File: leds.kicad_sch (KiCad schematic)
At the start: 67 parts, among them U4 TXB0101DRL

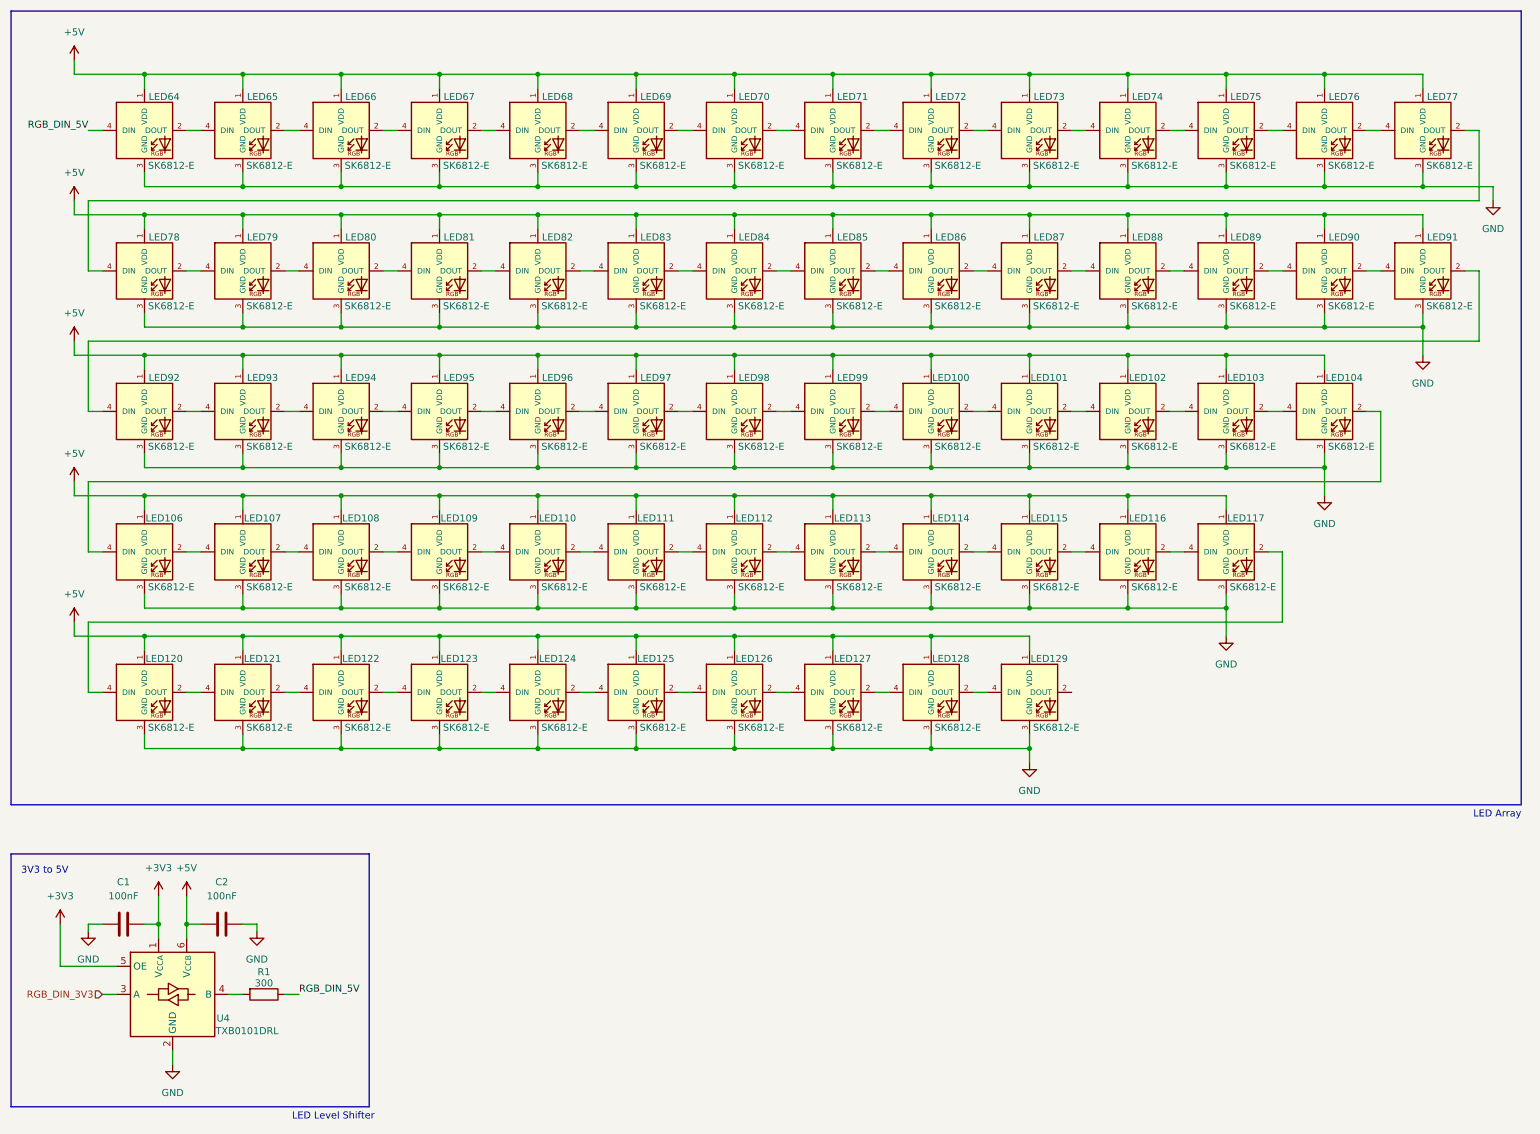
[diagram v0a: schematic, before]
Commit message: created v0.2 pcb
Started work on v0.2 pcb. Placed switches, LEDS, and Diodes. Working on MCU routing
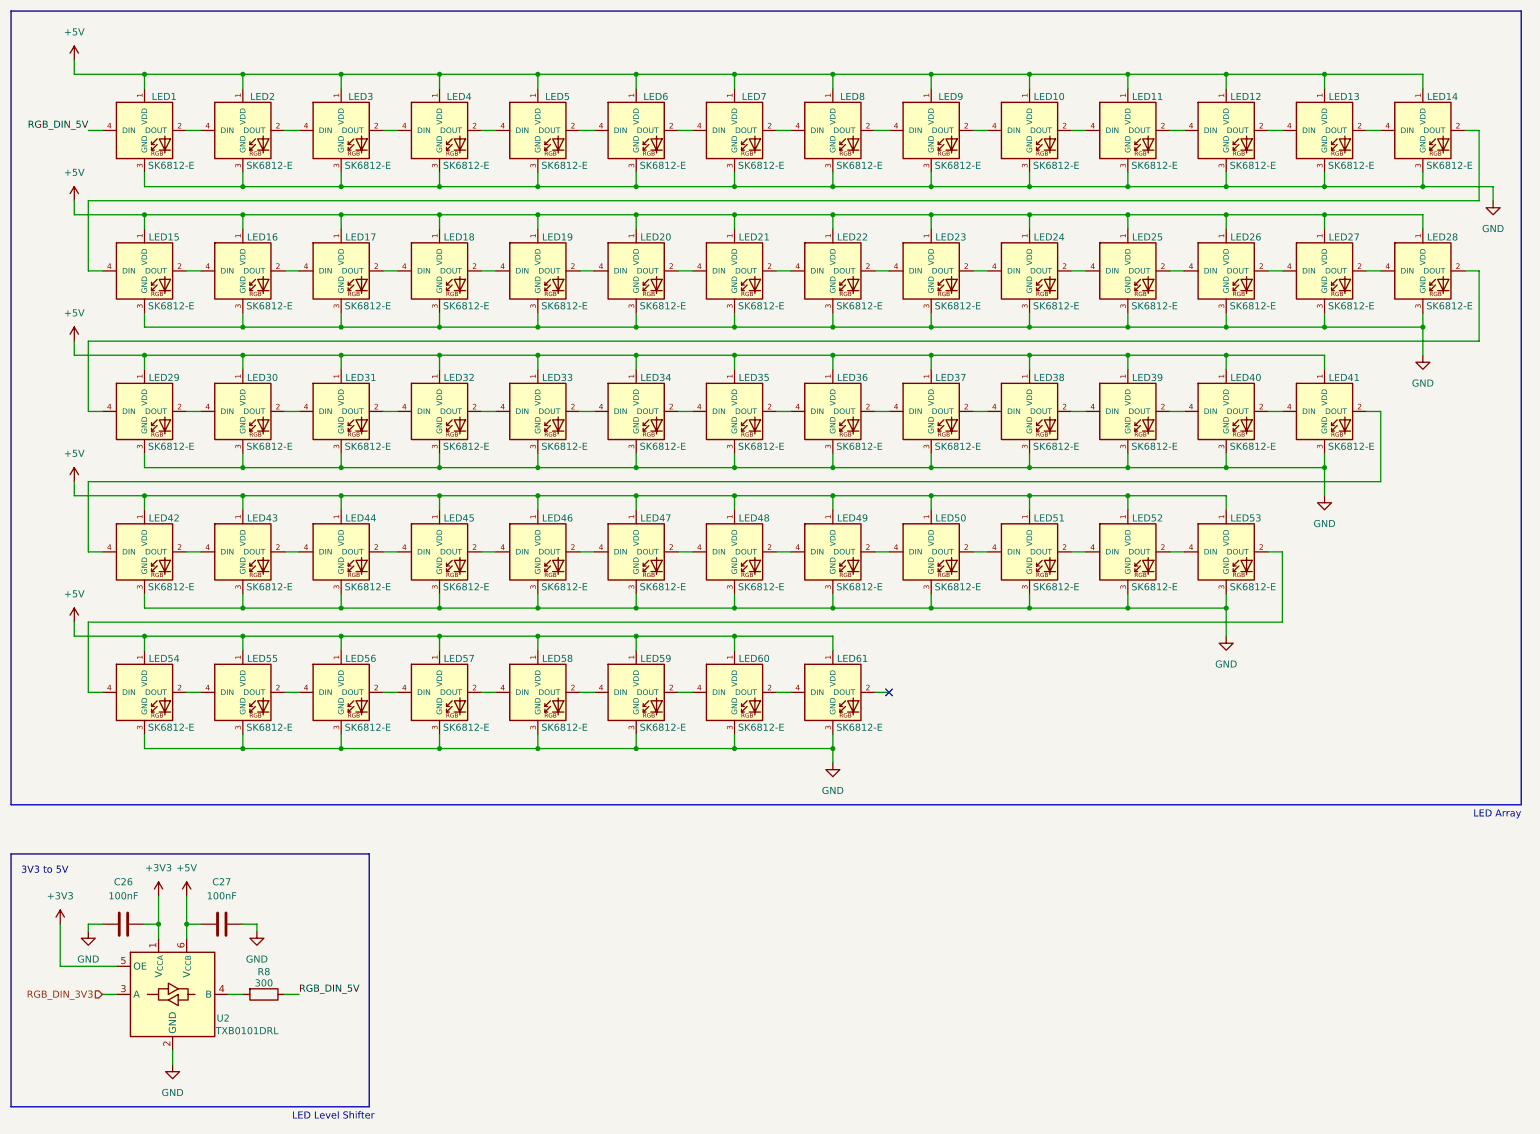
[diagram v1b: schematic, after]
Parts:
- removed LED128, LED129: SK6812-E, SK6812-E:LED_SK6812-E, symbol SK6812-E:SK6812-E
- C26: renamed from C1; footprint (none) -> Capacitor_SMD:C_0402_1005Metric
- C27: renamed from C2; footprint (none) -> Capacitor_SMD:C_0402_1005Metric
- LED1: renamed from LED64; footprint SK6812-E:LED_SK6812-E -> SamacSys_Parts:LED_SK6812-E
- LED10: renamed from LED73; footprint SK6812-E:LED_SK6812-E -> SamacSys_Parts:LED_SK6812-E
- LED11: renamed from LED74; footprint SK6812-E:LED_SK6812-E -> SamacSys_Parts:LED_SK6812-E
- LED12: renamed from LED75; footprint SK6812-E:LED_SK6812-E -> SamacSys_Parts:LED_SK6812-E
- LED13: renamed from LED76; footprint SK6812-E:LED_SK6812-E -> SamacSys_Parts:LED_SK6812-E
- LED14: renamed from LED77; footprint SK6812-E:LED_SK6812-E -> SamacSys_Parts:LED_SK6812-E
- LED15: renamed from LED78; footprint SK6812-E:LED_SK6812-E -> SamacSys_Parts:LED_SK6812-E
- LED16: renamed from LED79; footprint SK6812-E:LED_SK6812-E -> SamacSys_Parts:LED_SK6812-E
- LED17: renamed from LED80; footprint SK6812-E:LED_SK6812-E -> SamacSys_Parts:LED_SK6812-E
- LED18: renamed from LED81; footprint SK6812-E:LED_SK6812-E -> SamacSys_Parts:LED_SK6812-E
- LED19: renamed from LED82; footprint SK6812-E:LED_SK6812-E -> SamacSys_Parts:LED_SK6812-E
- LED2: renamed from LED65; footprint SK6812-E:LED_SK6812-E -> SamacSys_Parts:LED_SK6812-E
- LED20: renamed from LED83; footprint SK6812-E:LED_SK6812-E -> SamacSys_Parts:LED_SK6812-E
- LED21: renamed from LED84; footprint SK6812-E:LED_SK6812-E -> SamacSys_Parts:LED_SK6812-E
- LED22: renamed from LED85; footprint SK6812-E:LED_SK6812-E -> SamacSys_Parts:LED_SK6812-E
- LED23: renamed from LED86; footprint SK6812-E:LED_SK6812-E -> SamacSys_Parts:LED_SK6812-E
- LED24: renamed from LED87; footprint SK6812-E:LED_SK6812-E -> SamacSys_Parts:LED_SK6812-E
- LED25: renamed from LED88; footprint SK6812-E:LED_SK6812-E -> SamacSys_Parts:LED_SK6812-E
- LED26: renamed from LED89; footprint SK6812-E:LED_SK6812-E -> SamacSys_Parts:LED_SK6812-E
- LED27: renamed from LED90; footprint SK6812-E:LED_SK6812-E -> SamacSys_Parts:LED_SK6812-E
- LED28: renamed from LED91; footprint SK6812-E:LED_SK6812-E -> SamacSys_Parts:LED_SK6812-E
- LED29: renamed from LED92; footprint SK6812-E:LED_SK6812-E -> SamacSys_Parts:LED_SK6812-E
- LED3: renamed from LED66; footprint SK6812-E:LED_SK6812-E -> SamacSys_Parts:LED_SK6812-E
- LED30: renamed from LED93; footprint SK6812-E:LED_SK6812-E -> SamacSys_Parts:LED_SK6812-E
- LED31: renamed from LED94; footprint SK6812-E:LED_SK6812-E -> SamacSys_Parts:LED_SK6812-E
- LED32: renamed from LED95; footprint SK6812-E:LED_SK6812-E -> SamacSys_Parts:LED_SK6812-E
- LED33: renamed from LED96; footprint SK6812-E:LED_SK6812-E -> SamacSys_Parts:LED_SK6812-E
- LED34: renamed from LED97; footprint SK6812-E:LED_SK6812-E -> SamacSys_Parts:LED_SK6812-E
- LED35: renamed from LED98; footprint SK6812-E:LED_SK6812-E -> SamacSys_Parts:LED_SK6812-E
- LED36: renamed from LED99; footprint SK6812-E:LED_SK6812-E -> SamacSys_Parts:LED_SK6812-E
- LED37: renamed from LED100; footprint SK6812-E:LED_SK6812-E -> SamacSys_Parts:LED_SK6812-E
- LED38: renamed from LED101; footprint SK6812-E:LED_SK6812-E -> SamacSys_Parts:LED_SK6812-E
- LED39: renamed from LED102; footprint SK6812-E:LED_SK6812-E -> SamacSys_Parts:LED_SK6812-E
- LED4: renamed from LED67; footprint SK6812-E:LED_SK6812-E -> SamacSys_Parts:LED_SK6812-E
- LED40: renamed from LED103; footprint SK6812-E:LED_SK6812-E -> SamacSys_Parts:LED_SK6812-E
- LED41: renamed from LED104; footprint SK6812-E:LED_SK6812-E -> SamacSys_Parts:LED_SK6812-E
- LED42: renamed from LED106; footprint SK6812-E:LED_SK6812-E -> SamacSys_Parts:LED_SK6812-E
- LED43: renamed from LED107; footprint SK6812-E:LED_SK6812-E -> SamacSys_Parts:LED_SK6812-E
- LED44: renamed from LED108; footprint SK6812-E:LED_SK6812-E -> SamacSys_Parts:LED_SK6812-E
- LED45: renamed from LED109; footprint SK6812-E:LED_SK6812-E -> SamacSys_Parts:LED_SK6812-E
- LED46: renamed from LED110; footprint SK6812-E:LED_SK6812-E -> SamacSys_Parts:LED_SK6812-E
- LED47: renamed from LED111; footprint SK6812-E:LED_SK6812-E -> SamacSys_Parts:LED_SK6812-E
- LED48: renamed from LED112; footprint SK6812-E:LED_SK6812-E -> SamacSys_Parts:LED_SK6812-E
- LED49: renamed from LED113; footprint SK6812-E:LED_SK6812-E -> SamacSys_Parts:LED_SK6812-E
- LED5: renamed from LED68; footprint SK6812-E:LED_SK6812-E -> SamacSys_Parts:LED_SK6812-E
- LED50: renamed from LED114; footprint SK6812-E:LED_SK6812-E -> SamacSys_Parts:LED_SK6812-E
- LED51: renamed from LED115; footprint SK6812-E:LED_SK6812-E -> SamacSys_Parts:LED_SK6812-E
- LED52: renamed from LED116; footprint SK6812-E:LED_SK6812-E -> SamacSys_Parts:LED_SK6812-E
- LED53: renamed from LED117; footprint SK6812-E:LED_SK6812-E -> SamacSys_Parts:LED_SK6812-E
- LED54: renamed from LED120; footprint SK6812-E:LED_SK6812-E -> SamacSys_Parts:LED_SK6812-E
- LED55: renamed from LED121; footprint SK6812-E:LED_SK6812-E -> SamacSys_Parts:LED_SK6812-E
- LED56: renamed from LED122; footprint SK6812-E:LED_SK6812-E -> SamacSys_Parts:LED_SK6812-E
- LED57: renamed from LED123; footprint SK6812-E:LED_SK6812-E -> SamacSys_Parts:LED_SK6812-E
- LED58: renamed from LED124; footprint SK6812-E:LED_SK6812-E -> SamacSys_Parts:LED_SK6812-E
- LED59: renamed from LED125; footprint SK6812-E:LED_SK6812-E -> SamacSys_Parts:LED_SK6812-E
- LED6: renamed from LED69; footprint SK6812-E:LED_SK6812-E -> SamacSys_Parts:LED_SK6812-E
- LED60: renamed from LED126; footprint SK6812-E:LED_SK6812-E -> SamacSys_Parts:LED_SK6812-E
- LED61: renamed from LED127; footprint SK6812-E:LED_SK6812-E -> SamacSys_Parts:LED_SK6812-E
- LED7: renamed from LED70; footprint SK6812-E:LED_SK6812-E -> SamacSys_Parts:LED_SK6812-E
- LED8: renamed from LED71; footprint SK6812-E:LED_SK6812-E -> SamacSys_Parts:LED_SK6812-E
- LED9: renamed from LED72; footprint SK6812-E:LED_SK6812-E -> SamacSys_Parts:LED_SK6812-E
- R8: renamed from R1; footprint (none) -> Resistor_SMD:R_0402_1005Metric
- renumbered U4 to U2
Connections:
- no-connect marks 0 -> 1

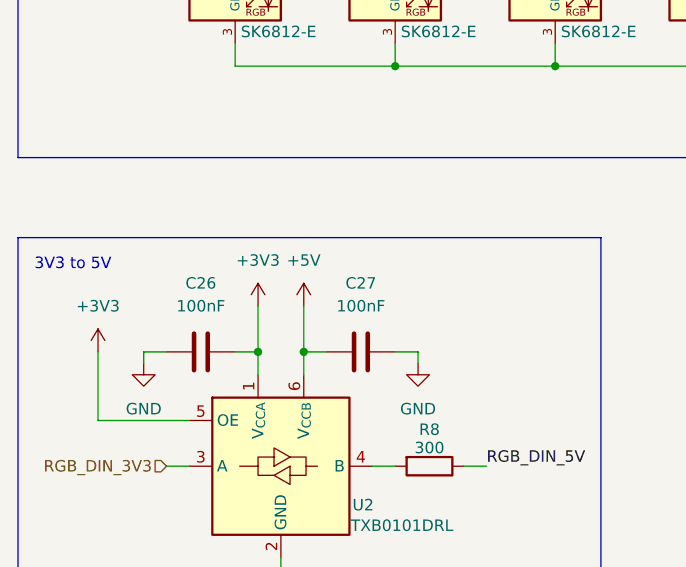
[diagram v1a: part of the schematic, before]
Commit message: work towards v0.2
Finished updating schematic. Ported to PCB editor. Need to rethink encoder.
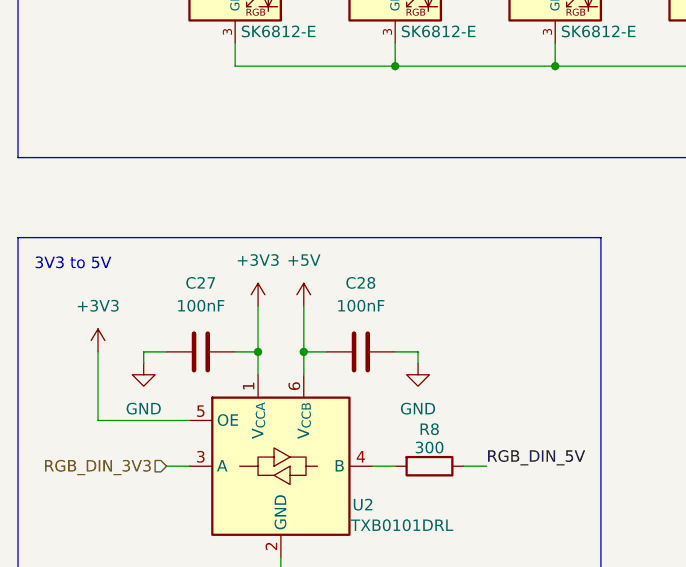
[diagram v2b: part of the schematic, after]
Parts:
- renumbered C26 to C27, C27 to C28
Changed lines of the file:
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@@
 		(dnp no)
 		(fields_autoplaced yes)
-		(property "Reference" "C27"
+		(property "Reference" "C28"
 			(at 111.76 205.74 90)
 			(effects
@@
 			(project "60WKeyboard"
 				(path "/a348110a-0b31-458b-8c85-d9f8cb2d19b6/5a1ec77c-d8b2-42c4-a20d-c6f1c8c10efc"
-					(reference "C27")
+					(reference "C28")
 					(unit 1)
 				)
@@
 		(dnp no)
 		(fields_autoplaced yes)
-		(property "Reference" "C26"
+		(property "Reference" "C27"
 			(at 93.98 205.74 90)
 			(effects
@@
 			(project ""
 				(path "/a348110a-0b31-458b-8c85-d9f8cb2d19b6/5a1ec77c-d8b2-42c4-a20d-c6f1c8c10efc"
-					(reference "C26")
+					(reference "C27")
 					(unit 1)
 				)

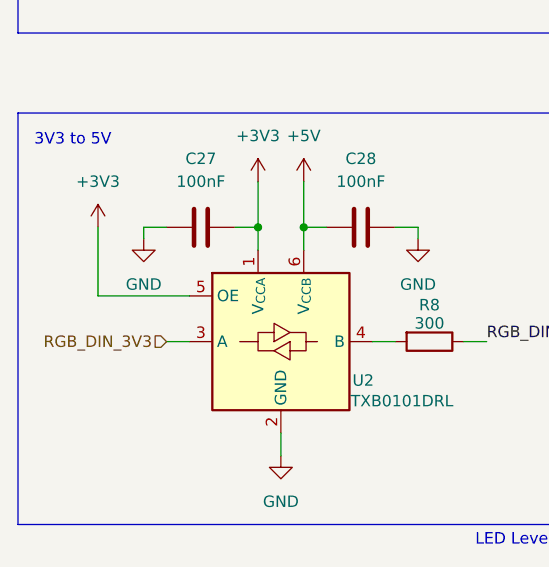
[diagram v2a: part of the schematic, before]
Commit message: v0.3
moving along
everything on board
need to wire chip and batt charger ic
switch matrix mostly done
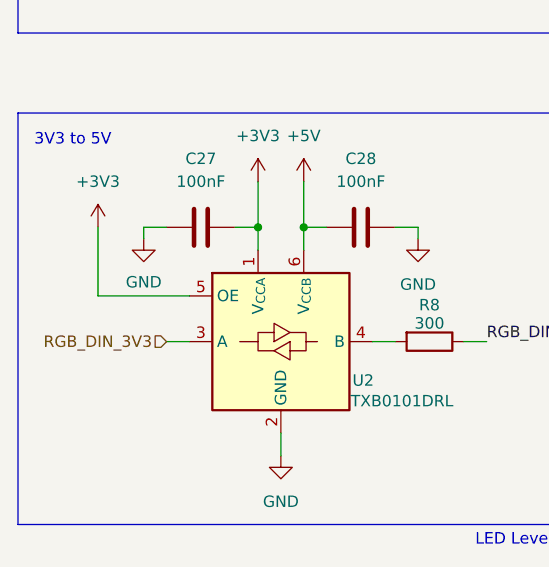
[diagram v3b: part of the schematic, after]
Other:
- title: (none) -> 60% Wireless Keyboard
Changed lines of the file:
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@@
 	(generator_version "9.0")
 	(paper "A3")
+	(title_block
+		(title "60% Wireless Keyboard")
+		(date "2025-09-20")
+		(rev "v0.3")
+	)
 	(rectangle
 		(start 73.66 48.26)
@@
 		(on_board yes)
 		(dnp no)
-		(fields_autoplaced yes)
 		(property "Reference" "#PWR057"
 			(at 87.63 220.98 0)
@@
 		)
 		(property "Value" "GND"
-			(at 87.63 219.71 0)
+			(at 87.63 219.456 0)
 			(effects
 				(font
